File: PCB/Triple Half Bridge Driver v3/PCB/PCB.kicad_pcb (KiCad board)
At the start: 2 copper layers, 363.5 x 231 mm, 267 parts, among them J1 Screw_Terminal_01x06, J10 Screw_Terminal_01x02, J11 Screw_Terminal_01x02, J12 Screw_Terminal_01x02, J13 Screw_Terminal_01x03, J14 Screw_Terminal_01x03, J15 Screw_Terminal_01x03, J16 Screw_Terminal_01x03, J17 Screw_Terminal_01x02, J18 Screw_Terminal_01x02, J19 Screw_Terminal_01x02, J2 Screw_Terminal_01x03, J20 Screw_Terminal_01x02, J21 Screw_Terminal_01x03, J22 Screw_Terminal_01x03, J3 Screw_Terminal_01x03, J4 Screw_Terminal_01x03, J5 Screw_Terminal_01x03, J6 Screw_Terminal_01x02, J7 Screw_Terminal_01x06, J8 Screw_Terminal_01x06, J9 Screw_Terminal_01x02, Q1 Q_PNP_BEC, Q10 IRF9540N, Q13 Q_PNP_BEC, Q14 IRF740, Q15 IRF740, Q16 Q_PNP_BEC, Q17 IRF740, Q18 IRF740, Q19 Q_PNP_BEC, Q2 Q_PNP_BEC, Q20 IRF740, Q21 IRF740, Q3 Q_PNP_BEC, Q4 IRF740, Q5 IRF740, Q6 IRF740, Q7 IRF740, Q8 IRF740, Q9 IRF740, SW1 SW_Push, U1 IRS2101, U10 IRS2101, U11 IRS2101, U12 IRS2101, U13 INA240A1D, U14 INA240A1D, U15 INA240A1D, U2 IRS2101, U3 IRS2101, U4 RaspberryPi_Pico, U5 LM7812_TO220, U6 LM7805_TO220, U7 INA240A1D, U8 INA240A1D, U9 INA240A1D

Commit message: Update PCB
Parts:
- removed the C1 at (185.6, 90.2)
- removed the C10 at (238.6, 104.2)
- removed the C26 at (238.6, 121.7)
- removed the C4 at (202.6, 100.7)
- removed the C52 at (243.6, 97.2)
- removed the C7 at (238.6, 115.7)
- removed the D1 at (197.0, 93.7)
- removed the D16 at (215.3, 118.2)
- removed the D4 at (215.3, 101.7)
- removed the Q1 at (196.6, 119.2)
- removed the Q4 at (230.2, 101.1)
- removed the Q5 at (230.1, 113.6)
- removed the R1 at (172.6, 90.9)
- removed the R10 at (215.3, 107.7)
- removed the R2 at (172.6, 102.9)
- removed the R53 at (215.0, 96.2)
- removed the R56 at (215.3, 112.7)
- removed the R59 at (245.1, 109.7)
- removed the R60 at (226.8, 125.2)
- removed the R7 at (202.6, 113.2)
- removed the TP1 at (180.6, 97.7)
- removed the TP2 at (180.6, 105.7)
- removed the TP7 at (208.6, 95.7)
- removed the TP8 at (209.0, 112.5)
- removed the U1 at (189.5, 98.9)
- added C29: C, Capacitor_THT:C_Rect_L7.0mm_W4.5mm_P5.00mm, F.Cu at (195.3, 75.1)
- added C3: 4.7uF 35V, Capacitor_THT:C_Rect_L7.0mm_W4.5mm_P5.00mm, F.Cu at (158.3, 71.1)
- added C30: C, Capacitor_THT:C_Rect_L7.0mm_W4.5mm_P5.00mm, F.Cu at (200.3, 86.1)
- added C51: C, Capacitor_THT:C_Rect_L7.0mm_W4.5mm_P5.00mm, F.Cu at (200.3, 69.6)
- added C6: C, Capacitor_THT:C_Rect_L7.0mm_W4.5mm_P5.00mm, F.Cu at (172.8, 76.1)
- added C9: C, Capacitor_THT:C_Rect_L7.0mm_W4.5mm_P5.00mm, F.Cu at (195.3, 80.6)
- added D18: D_Schottky, Diode_THT:D_A-405_P7.62mm_Horizontal, F.Cu at (177.8, 81.9)
- added D3: D, Diode_THT:D_A-405_P7.62mm_Horizontal, F.Cu at (168.8, 71.6)
- added D6: D_Schottky, Diode_THT:D_A-405_P7.62mm_Horizontal, F.Cu at (177.8, 73.7)
- added J23: Screw_Terminal_01x01, Connector_PinHeader_2.54mm:PinHeader_1x01_P2.54mm_Vertical, F.Cu at (113.0, 70.5)
- added J24: Screw_Terminal_01x03, 3 Pin Spring Terminal:1792876, F.Cu at (246.0, 202.5)
- added J25: Screw_Terminal_01x03, 3 Pin Spring Terminal:1792876, F.Cu at (217.0, 203.0)
- added J26: Screw_Terminal_01x02, Connector_PinHeader_2.54mm:PinHeader_1x02_P2.54mm_Vertical, F.Cu at (197.0, 160.2)
- added J28: Screw_Terminal_01x01, Connector_PinHeader_2.54mm:PinHeader_1x01_P2.54mm_Vertical, F.Cu at (64.5, 68.0)
- added Q3: Q_PNP_BEC, Package_TO_SOT_THT:TO-220-3_Vertical, F.Cu at (167.3, 88.1)
- added Q8: IRF740, Package_TO_SOT_THT:TO-220-3_Vertical, F.Cu at (189.8, 70.1)
- added Q9: IRF740, Package_TO_SOT_THT:TO-220-3_Vertical, F.Cu at (189.8, 81.6)
- added R12: R, Resistor_THT:R_Axial_DIN0207_L6.3mm_D2.5mm_P7.62mm_Horizontal, F.Cu at (177.8, 77.8)
- added R5: R, Resistor_THT:R_Axial_DIN0207_L6.3mm_D2.5mm_P7.62mm_Horizontal, F.Cu at (157.8, 83.4)
- added R55: R, Resistor_THT:R_Axial_DIN0207_L6.3mm_D2.5mm_P7.62mm_Horizontal, F.Cu at (177.8, 69.6)
- added R58: R, Resistor_THT:R_Axial_DIN0207_L6.3mm_D2.5mm_P7.62mm_Horizontal, F.Cu at (177.8, 86.0)
- added R6: R, Resistor_THT:R_Axial_DIN0207_L6.3mm_D2.5mm_P7.62mm_Horizontal, F.Cu at (153.6, 75.8)
- added R63: R, Resistor_THT:R_Axial_DIN0207_L6.3mm_D2.5mm_P7.62mm_Horizontal, F.Cu at (185.4, 90.1)
- added R64: R, Resistor_THT:R_Axial_DIN0207_L6.3mm_D2.5mm_P7.62mm_Horizontal, F.Cu at (189.5, 91.6)
- added R78: R, Resistor_THT:R_Axial_DIN0207_L6.3mm_D2.5mm_P7.62mm_Horizontal, F.Cu at (59.8, 130.8)
- added R79: R, Resistor_THT:R_Axial_DIN0207_L6.3mm_D2.5mm_P7.62mm_Horizontal, F.Cu at (123.9, 171.0)
- added R80: R, Resistor_THT:R_Axial_DIN0207_L6.3mm_D2.5mm_P7.62mm_Horizontal, F.Cu at (131.5, 167.0)
- added R9: R, Resistor_THT:R_Axial_DIN0207_L6.3mm_D2.5mm_P7.62mm_Horizontal, F.Cu at (149.3, 83.4)
- added RV2: R_Potentiometer, Potentiometer_THT:Potentiometer_Omeg_PC16BU_Vertical, F.Cu at (106.0, 146.5)
- added RV3: R_Potentiometer, Potentiometer_THT:Potentiometer_Omeg_PC16BU_Vertical, F.Cu at (124.5, 146.5)
- added SW2: SW_Push, Button_Switch_THT:SW_PUSH_6mm_H8.5mm, F.Cu at (64.0, 141.9)
- added TP11: TestPoint, TestPoint:TestPoint_THTPad_2.0x2.0mm_Drill1.0mm, F.Cu at (172.8, 71.6)
- added TP12: TestPoint, TestPoint:TestPoint_THTPad_2.0x2.0mm_Drill1.0mm, F.Cu at (172.8, 85.1)
- added TP5: TestPoint, TestPoint:TestPoint_THTPad_2.0x2.0mm_Drill1.0mm, F.Cu at (149.3, 87.6)
- added TP6: TestPoint, TestPoint:TestPoint_THTPad_2.0x2.0mm_Drill1.0mm, F.Cu at (149.3, 71.1)
- added U3: IRS2101, Package_DIP:DIP-8_W7.62mm, F.Cu at (161.0, 75.8)
- J10, J9: footprint 3 Pin Spring Terminal:1792863 -> Connector_PinHeader_2.54mm:PinHeader_1x02_P2.54mm_Vertical
- moved C48 181.7 mm to (207.0, 148.5), turned to 0 degrees
- moved C25 167.3 mm to (207.0, 73.3)
- moved C13 166.5 mm to (212.0, 143.0), turned to 180 degrees
- moved C23 162.0 mm to (212.0, 78.8)
- moved R52 159.3 mm to (217.8, 67.8), turned to 180 degrees
- moved Q14 159.2 mm to (217.5, 148.0), turned to 90 degrees
- moved C12 158.8 mm to (212.0, 137.5), turned to 180 degrees
- moved C14 158.7 mm to (207.0, 132.0)
- moved C50 157.6 mm to (207.0, 89.8), turned to 0 degrees
- moved C49 156.4 mm to (207.0, 119.1), turned to 0 degrees
- moved R51 155.6 mm to (221.9, 69.3), turned to 0 degrees
- moved R35 154.3 mm to (221.9, 128.0), turned to 0 degrees
- moved C24 151.2 mm to (212.0, 84.3), turned to 180 degrees
- moved C20 149.0 mm to (207.0, 102.6)
- moved Q15 146.8 mm to (217.5, 136.5), turned to 90 degrees
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- renumbered C3 to C1, C29 to C10, C30 to C26, C6 to C4, C51 to C52, C9 to C7, D3 to D1, D18 to D16, D6 to D4, Q3 to Q1, Q8 to Q4, Q9 to Q5, R5 to R1, R12 to R10, R6 to R2, R55 to R53, R58 to R56, R63 to R59, R64 to R60, R9 to R7, TP5 to TP1, TP6 to TP2, TP11 to TP7, TP12 to TP8, U3 to U1
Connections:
- net Button  renamed Button 1
- net Potentiometer renamed Potentiometer 1
- C34 pad 1: +5V -> Net-(J26-Pin_1)
- C35 pad 1: Net-(Q10-G) -> VSS
- C35 pad 2: Net-(D25-K) -> Net-(Q10-G)
- C4 pad 2: Motor 2A -> Motor 2B
- C52 pad 2: High 2A2 -> High 2B2
- C7 pad 1: Low 2A2 -> Low 2B2
- D16 pad 1: Low 2A1 -> Low 2B1
- D16 pad 2: Low 2A2 -> Low 2B2
- D4 pad 1: High 2A1 -> High 2B1
- D4 pad 2: High 2A2 -> High 2B2
- Q4 pad 1: High 2A2 -> High 2B2
- Q4 pad 3: Motor 2A -> Motor 2B
- Q5 pad 1: Low 2A2 -> Low 2B2
- Q5 pad 2: Motor 2A -> Motor 2B
- R1 pad 2: Gate 2AH -> Gate 2BH
- R10 pad 1: Low 2A1 -> Low 2B1
- R10 pad 2: Low 2A2 -> Low 2B2
- R2 pad 1: Gate 2AL -> Gate 2BL
- R53 pad 1: High 2A1 -> High 2B1
- R53 pad 2: High 2A2 -> High 2B2
- R56 pad 2: Low 2A2 -> Low 2B2
- R59 pad 2: Motor 2A -> Motor 2B
- R60 pad 1: Motor 2A -> Motor 2B
- R7 pad 1: Low 2A1 -> Low 2B1
- TP1 pad 1: Gate 2AH -> Gate 2BH
- TP2 pad 1: Gate 2AL -> Gate 2BL
- TP7 pad 1: High 2A1 -> High 2B1
- TP8 pad 1: Low 2A1 -> Low 2B1
- U1 pad 2: Gate 2AH -> Gate 2BH
- U1 pad 3: Gate 2AL -> Gate 2BL
- U1 pad 5: Low 2A1 -> Low 2B1
- U1 pad 6: Motor 2A -> Motor 2B
- U1 pad 7: High 2A1 -> High 2B1
- U4 pad 1: unconnected-(U4-GPIO0-Pad1) -> Button 2
- U4 pad 32: unconnected-(U4-GPIO27_ADC1-Pad32) -> Potentiometer 2
- U4 pad 34: unconnected-(U4-GPIO28_ADC2-Pad34) -> Potentiometer 3
- U4 pad 40: unconnected-(U4-VBUS-Pad40) -> Net-(J23-Pin_1)
- U6 pad 3: +5V -> Net-(J26-Pin_1)
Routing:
- net GND1: track 666.9 -> 7.05 mm
- net GND: track 469.5 -> 30.2 mm, vias 0 -> 1
- net VPP: track 469.4 -> 112.0 mm, vias 2 -> 3
- net +5V: track 316.4 -> 61.8 mm
- net +3V3: track 363.9 -> 116.8 mm, vias 1 -> 0
- net Gate 1CH: track 30.4 -> 217.2 mm, vias 0 -> 1
- net Gate 1BL: track 28.9 -> 186.6 mm, vias 0 -> 1
- net Motor 2B: track 99.2 -> 255.5 mm, vias 0 -> 2
- net Gate 1BH: track 28.4 -> 182.4 mm, vias 0 -> 3
- net Motor 2A: track 115.2 -> 257.5 mm, vias 0 -> 1
- net Gate 2BL: track 32.9 -> 165.7 mm, vias 0 -> 2
- net Gate 2AL: track 31.3 -> 161.3 mm
- net Motor 1C: track 108.4 -> 236.2 mm, vias 0 -> 2
- net Gate 2CH: track 30.4 -> 152.8 mm, vias 0 -> 3
- net Gate 1CL: track 30.9 -> 149.2 mm, vias 0 -> 1
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- added copper zone on B.Cu, net +3V3
- added copper zone on B.Cu, net VPP
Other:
- board size 363.5 x 231 mm -> 221.5 x 155.5 mm

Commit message: Slightly optimize PCB tracks
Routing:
- net Motor 1B: track 167.7 -> 163.0 mm
- net LED 2: track 47.5 -> 42.9 mm
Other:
- board size 221.5 x 155.5 mm -> 221.5 x 150.5 mm
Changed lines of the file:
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@@
 	)
 	(gr_rect
-		(start 46.5 60)
-		(end 268 215.5)
+		(start 47.5 62)
+		(end 269 212.5)
 		(stroke
 			(width 0.15)
@@
 	)
 	(segment
-		(start 179.7067 151.138)
-		(end 182.2631 151.138)
-		(width 1.1)
-		(layer "B.Cu")
-		(net 4)
-	)
-	(segment
 		(start 177.855 151.138)
-		(end 179.7067 151.138)
+		(end 182.2631 151.138)
 		(width 1.1)
 		(layer "B.Cu")
@@
 	(segment
 		(start 246 202.5)
-		(end 246 200.6233)
+		(end 246 199.5976)
 		(width 1.1)
 		(layer "B.Cu")
@@
 	)
 	(segment
-		(start 246 199.5976)
-		(end 246 200.6233)
-		(width 1.1)
-		(layer "B.Cu")
-		(net 16)
-	)
-	(segment
 		(start 231.9483 134.6027)
 		(end 231.9483 131.8764)
@@
 	)
 	(segment
-		(start 240.5716 108.7356)
-		(end 240.3524 108.7356)
-		(width 1.1)
-		(layer "B.Cu")
-		(net 18)
-	)
-	(segment
 		(start 229.8836 100.4807)
 		(end 229.5 100.4807)
@@
 	)
 	(segment
-		(start 238.72 107.889)
-		(end 240.5717 107.889)
-		(width 1.1)
-		(layer "B.Cu")
-		(net 18)
-	)
-	(segment
 		(start 255.6017 132.9663)
 		(end 255.6017 136.855)
@@
 	)
 	(segment
-		(start 240.5717 108.7355)
-		(end 240.5716 108.7356)
-		(width 1.1)
-		(layer "B.Cu")
-		(net 18)
-	)
-	(segment
 		(start 260.441 152.7242)
 		(end 260.441 155.7094)
@@
 	)
 	(segment
-		(start 239.6941 108.0773)
-		(end 237.7459 108.0773)
-		(width 1.1)
-		(layer "B.Cu")
-		(net 18)
-	)
-	(segment
-		(start 237.7459 108.0773)
+		(start 236.3259 109.4549)
 		(end 236.3683 109.4549)
 		(width 1.1)
@@
 	)
 	(segment
-		(start 236.3259 109.4549)
-		(end 236.3683 109.4549)
+		(start 238.72 107.889)
+		(end 237.9342 107.889)
 		(width 1.1)
 		(layer "B.Cu")
@@
 	)
 	(segment
-		(start 240.5717 107.889)
-		(end 240.5717 108.7355)
+		(start 234.5 107.629)
+		(end 236.3259 109.4549)
 		(width 1.1)
 		(layer "B.Cu")
@@
 	)
 	(segment
-		(start 234.5 107.629)
-		(end 236.3259 109.4549)
+		(start 260.5521 141.8054)
+		(end 260.5521 152.6131)
 		(width 1.1)
 		(layer "B.Cu")
@@
 	)
 	(segment
-		(start 260.5521 141.8054)
-		(end 260.5521 152.6131)
+		(start 237.9342 107.889)
+		(end 236.3683 109.4549)
 		(width 1.1)
 		(layer "B.Cu")
@@
 	)
 	(segment
-		(start 240.3524 108.7356)
-		(end 239.6941 108.0773)
-		(width 1.1)
-		(layer "B.Cu")
-		(net 18)
-	)
-	(segment
 		(start 221.88 98.629)
 		(end 218.7128 98.629)
@@
 	)
 	(segment
-		(start 256.7483 196.25)
-		(end 256.1558 196.25)
-		(width 1.1)
-		(layer "F.Cu")
-		(net 49)
-	)
-	(segment
-		(start 258.7 196.25)
-		(end 256.7483 196.25)
+		(start 256.1558 196.25)
+		(end 258.7 196.25)
 		(width 1.1)
 		(layer "F.Cu")
@@
 	)
 	(segment
-		(start 79.5 187)
-		(end 76.7467 187)
-		(width 0.25)
-		(layer "F.Cu")
-		(net 67)
-	)
-	(segment
-		(start 76.0034 186.82)
-		(end 75.44 186.82)
-		(width 0.25)
-		(layer "F.Cu")
-		(net 67)
-	)
-	(segment
 		(start 67.08 184.6233)
 		(end 67.08 186.82)
@@
 	)
 	(segment
-		(start 76.7467 187)
-		(end 76.5667 186.82)
+		(start 75.62 187)
+		(end 75.44 186.82)
 		(width 0.25)
 		(layer "F.Cu")
@@
 	)
 	(segment
-		(start 76.0034 186.82)
-		(end 76.5667 186.82)
+		(start 75.44 186.82)
+		(end 71.26 186.82)
 		(width 0.25)
 		(layer "F.Cu")
@@
 	)
 	(segment
-		(start 75.44 186.82)
-		(end 71.26 186.82)
+		(start 79.5 187)
+		(end 75.62 187)
 		(width 0.25)
 		(layer "F.Cu")
@@
 	)
 	(segment
-		(start 66.2466 206.1933)
-		(end 67.08 206.1933)
+		(start 67.08 207.0267)
+		(end 67.08 207.32)
 		(width 0.25)
 		(layer "F.Cu")
@@
 	)
 	(segment
-		(start 67.08 207.32)
-		(end 67.08 206.1933)
-		(width 0.25)
-		(layer "F.Cu")
-		(net 70)
-	)
-	(segment
 		(start 71.26 207.32)
 		(end 75.44 207.32)
@@
 	)
 	(segment
-		(start 63.58 202.7)
-		(end 63.58 203.5267)
-		(width 0.25)
-		(layer "F.Cu")
-		(net 70)
-	)
-	(segment
 		(start 75.44 207.32)
 		(end 76.5667 207.32)
@@
 	(segment
 		(start 63.58 203.5267)
-		(end 66.2466 206.1933)
+		(end 67.08 207.0267)
 		(width 0.25)
 		(layer "F.Cu")
@@
 	)
 	(segment
-		(start 66.58 195.4)
-		(end 65.9067 195.4)
+		(start 63.58 202.7)
+		(end 63.58 203.5267)
 		(width 0.25)
 		(layer "F.Cu")
@@
 	)
 	(segment
-		(start 65.9067 195.4)
-		(end 64.9067 194.4)
+		(start 66.58 195.4)
+		(end 65.9067 195.4)
 		(width 0.25)
 		(layer "F.Cu")
@@
 	)
 	(segment
-		(start 65.9533 205.0666)
-		(end 67.08 206.1933)
+		(start 65.9067 195.4)
+		(end 64.9067 194.4)
 		(width 0.25)
-		(layer "B.Cu")
+		(layer "F.Cu")
 		(net 70)
 	)
 	(segment
-		(start 65.9533 196.0267)
-		(end 65.9533 205.0666)
+		(start 66.58 195.4)
+		(end 65.9533 196.0267)
 		(width 0.25)
 		(layer "B.Cu")
@@
 	)
 	(segment
-		(start 67.08 207.32)
-		(end 67.08 206.1933)
+		(start 65.9533 206.1933)
+		(end 67.08 207.32)
 		(width 0.25)
 		(layer "B.Cu")
@@
 	)
 	(segment
-		(start 66.58 195.4)
-		(end 65.9533 196.0267)
+		(start 65.9533 196.0267)
+		(end 65.9533 206.1933)
 		(width 0.25)
 		(layer "B.Cu")
@@
 	)
 	(segment
-		(start 72.6987 135.0213)
-		(end 89.22 118.5)
+		(start 58.6 144.4)
+		(end 67.9787 135.0213)
 		(width 0.25)
 		(layer "B.Cu")
@@
 	)
 	(segment
-		(start 72.6987 142.8013)
-		(end 72.6987 135.0213)
+		(start 72.6987 135.0213)
+		(end 89.22 118.5)
 		(width 0.25)
 		(layer "B.Cu")
@@
 	)
 	(segment
-		(start 71.1 144.4)
-		(end 72.6987 142.8013)
+		(start 57.05 144.4)
+		(end 58.6 144.4)
 		(width 0.25)
 		(layer "B.Cu")
@@
 	)
 	(segment
-		(start 57.05 144.4)
-		(end 71.1 144.4)
+		(start 67.9787 135.0213)
+		(end 72.6987 135.0213)
 		(width 0.25)
 		(layer "B.Cu")
@@
 	)
 	(segment
+		(start 80.9133 178.2533)
+		(end 79.2125 178.2533)
+		(width 0.25)
+		(layer "B.Cu")
+		(net 110)
+	)
+	(segment
 		(start 83.42 178)
 		(end 82.04 179.38)
@@
 	)
 	(segment
-		(start 80.9133 179.38)
-		(end 80.9133 179.0982)
+		(start 76.6907 175.7315)
+		(end 76.6907 167.156)
 		(width 0.25)
 		(layer "B.Cu")
@@
 	)
 	(segment
-		(start 80.0684 178.2533)
-		(end 79.2125 178.2533)
+		(start 76.6907 167.156)
+		(end 82.04 161.8067)
 		(width 0.25)
 		(layer "B.Cu")
@@
 	)
 	(segment
-		(start 76.6907 175.7315)
-		(end 76.6907 167.156)
-		(width 0.25)
-		(layer "B.Cu")
-		(net 110)
-	)
-	(segment
 		(start 128.765 159)
 		(end 128.765 160.1767)
@@
 	)
 	(segment
-		(start 82.04 179.38)
-		(end 80.9133 179.38)
+		(start 79.2125 178.2533)
+		(end 76.6907 175.7315)
 		(width 0.25)
 		(layer "B.Cu")
@@
 	(segment
 		(start 128.965 163)
-		(end 128.965 164.1767)
-		(width 0.25)
-		(layer "B.Cu")
-		(net 110)
-	)
-	(segment
-		(start 128.765 160.1767)
-		(end 128.965 160.3767)
-		(width 0.25)
-		(layer "B.Cu")
-		(net 110)
-	)
-	(segment
-		(start 99.3 181.52)
-		(end 100.715 182.935)
+		(end 128.965 164.7295)
 		(width 0.25)
 		(layer "B.Cu")
@@
 	)
 	(segment
-		(start 80.9133 179.0982)
-		(end 80.0684 178.2533)
+		(start 82.04 179.38)
+		(end 80.9133 178.2533)
 		(width 0.25)
 		(layer "B.Cu")
@@
 	)
 	(segment
-		(start 82.04 160.68)
-		(end 82.04 161.8067)
+		(start 128.765 160.1767)
+		(end 128.965 160.3767)
 		(width 0.25)
 		(layer "B.Cu")
@@
 	)
 	(segment
-		(start 128.965 164.1767)
-		(end 128.965 164.7295)
+		(start 99.3 181.52)
+		(end 100.715 182.935)
 		(width 0.25)
 		(layer "B.Cu")
@@
 	)
 	(segment
-		(start 76.6907 167.156)
-		(end 82.04 161.8067)
+		(start 82.04 161.8067)
+		(end 82.04 160.68)
 		(width 0.25)
 		(layer "B.Cu")
@@
 		(width 0.25)
 		(layer "B.Cu")
-		(net 110)
-	)
-	(segment
-		(start 79.2125 178.2533)
-		(end 76.6907 175.7315)
-		(width 0.25)
-		(layer "B.Cu")

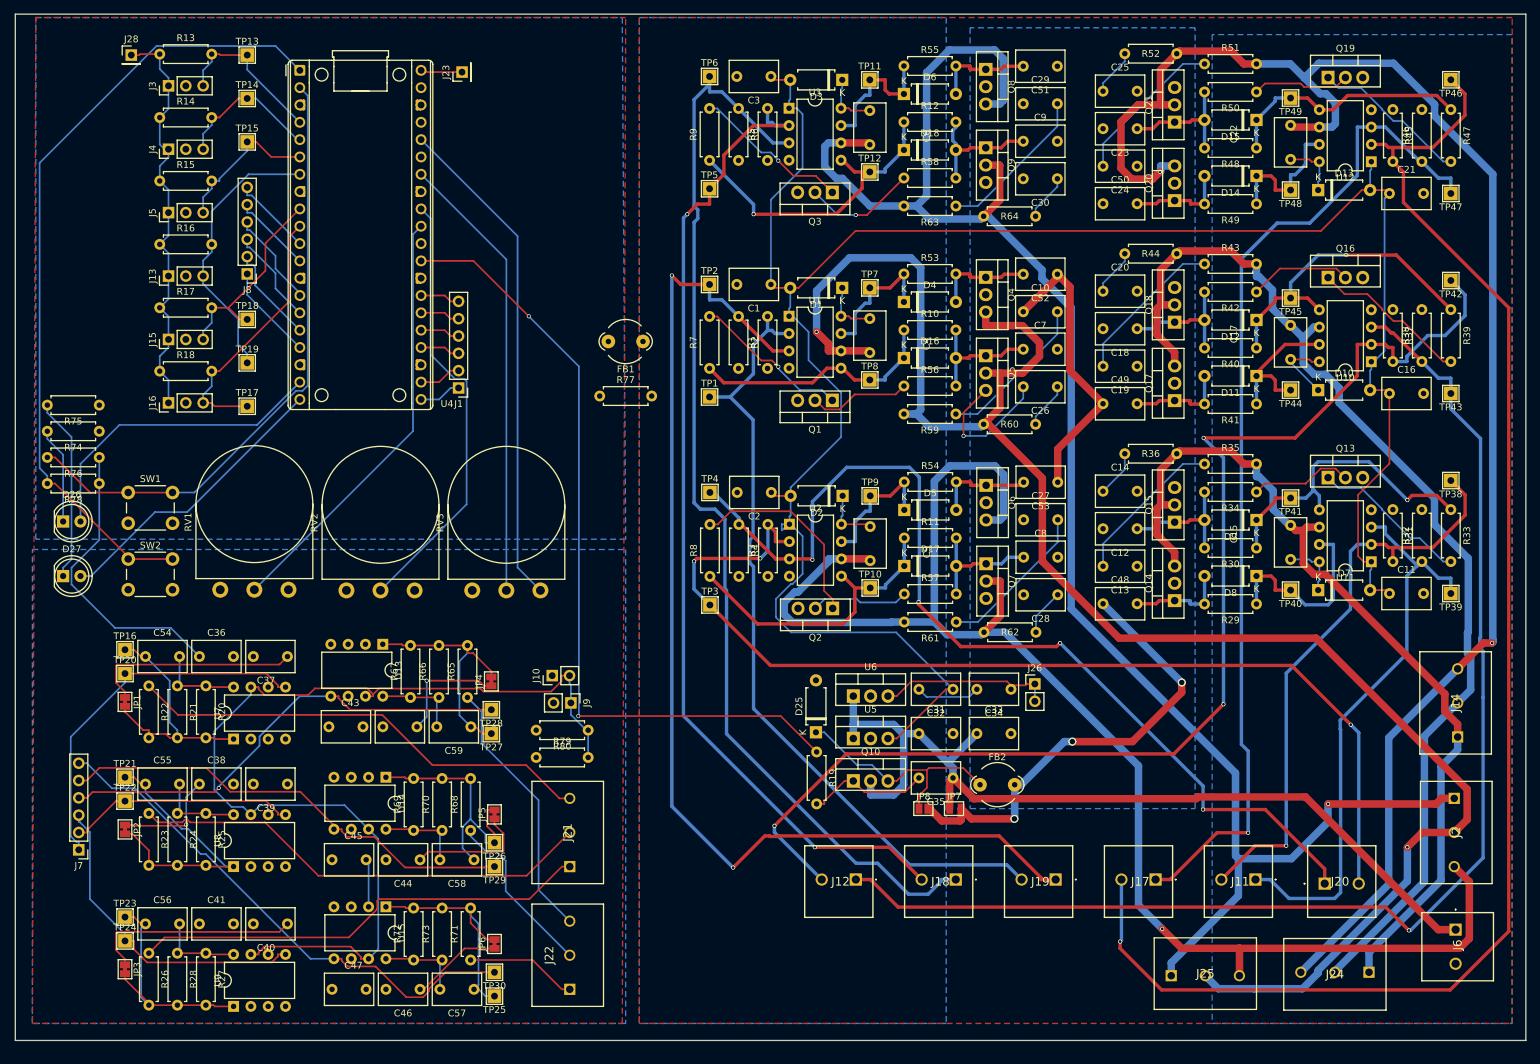
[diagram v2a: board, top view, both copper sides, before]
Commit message: Fix potentiometer footprint and overlapping silkscreen on PCB
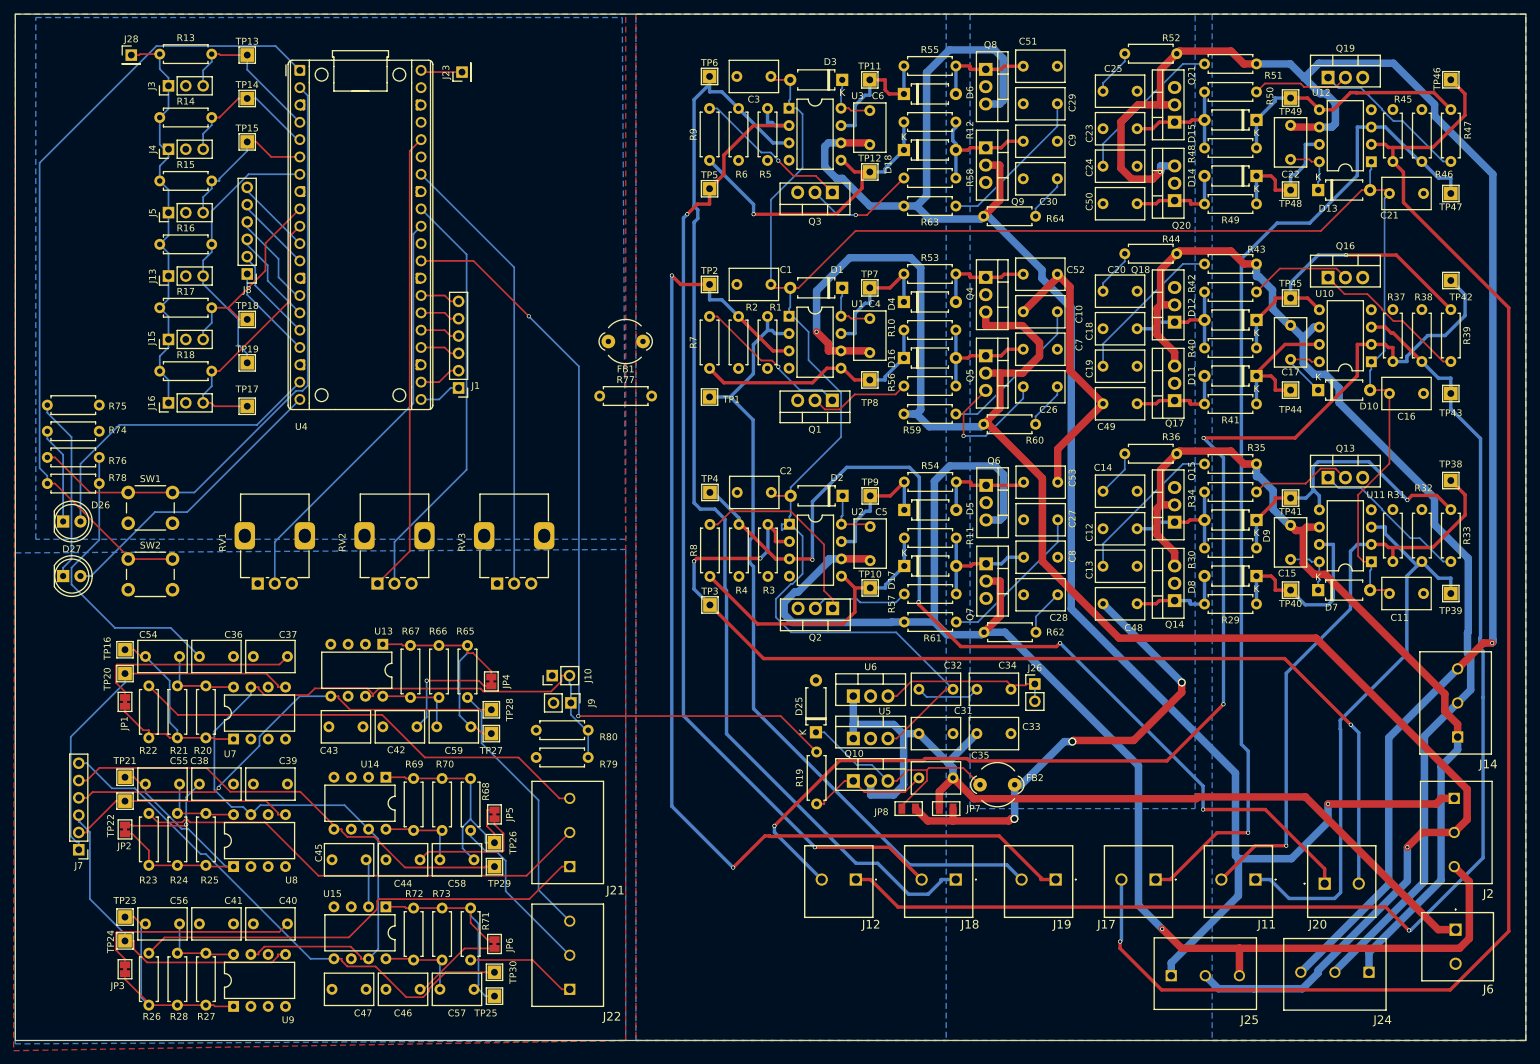
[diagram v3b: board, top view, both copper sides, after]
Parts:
- RV1, RV2, RV3: footprint Potentiometer_THT:Potentiometer_Omeg_PC16BU_Vertical -> Potentiometer_THT:Potentiometer_Alps_RK09K_Single_Vertical
- moved RV3 6.43 mm to (118.2, 145.5)
- moved RV2 5.54 mm to (100.6, 145.5)
- moved RV1 4.59 mm to (83.0, 145.5)
- moved JP8 2.15 mm to (178.5, 178.5)
- moved JP7 1.15 mm to (184.0, 178.5)
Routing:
- net +3V3: track 116.8 -> 111.2 mm
- net Potentiometer 2: track 64.7 -> 62.1 mm
- net Potentiometer 1: track 63.4 -> 61.3 mm
- net VPP: track 112.0 -> 113.7 mm
- net Net-(D25-K): track 35.0 -> 36.0 mm
- net VSS: track 133.8 -> 134.5 mm
- net Potentiometer 3: track 66.2 -> 65.7 mm
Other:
- board text added: "C42"
